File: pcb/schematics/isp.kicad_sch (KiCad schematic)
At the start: 23 parts, among them J3 Conn_02x07_Counter_Clockwise

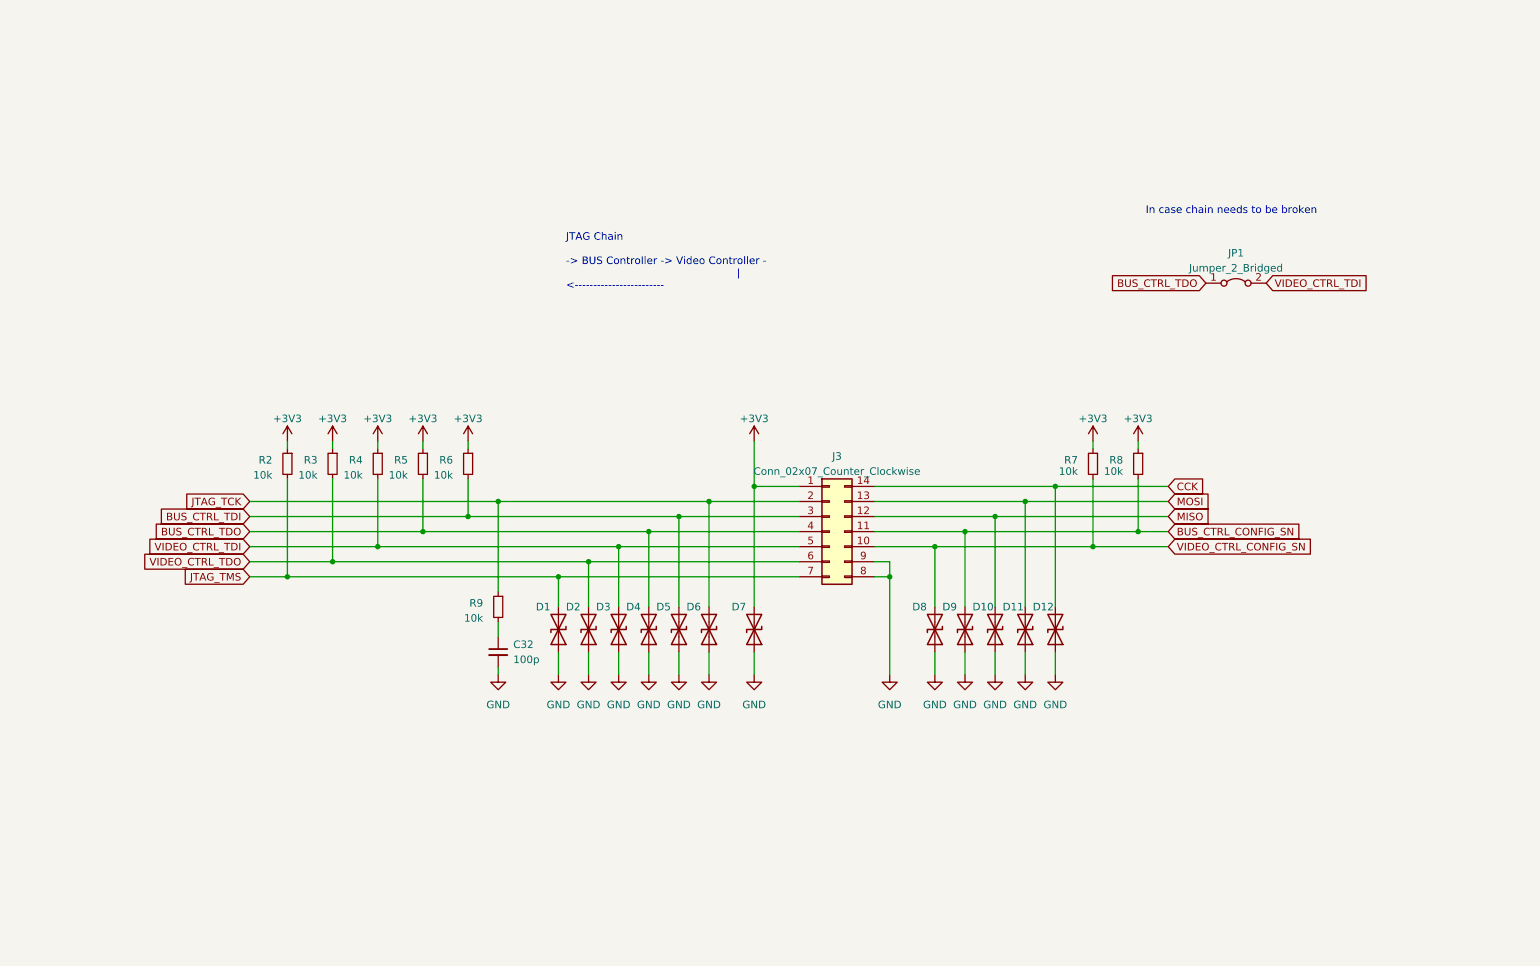
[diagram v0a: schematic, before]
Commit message: add the programming controller
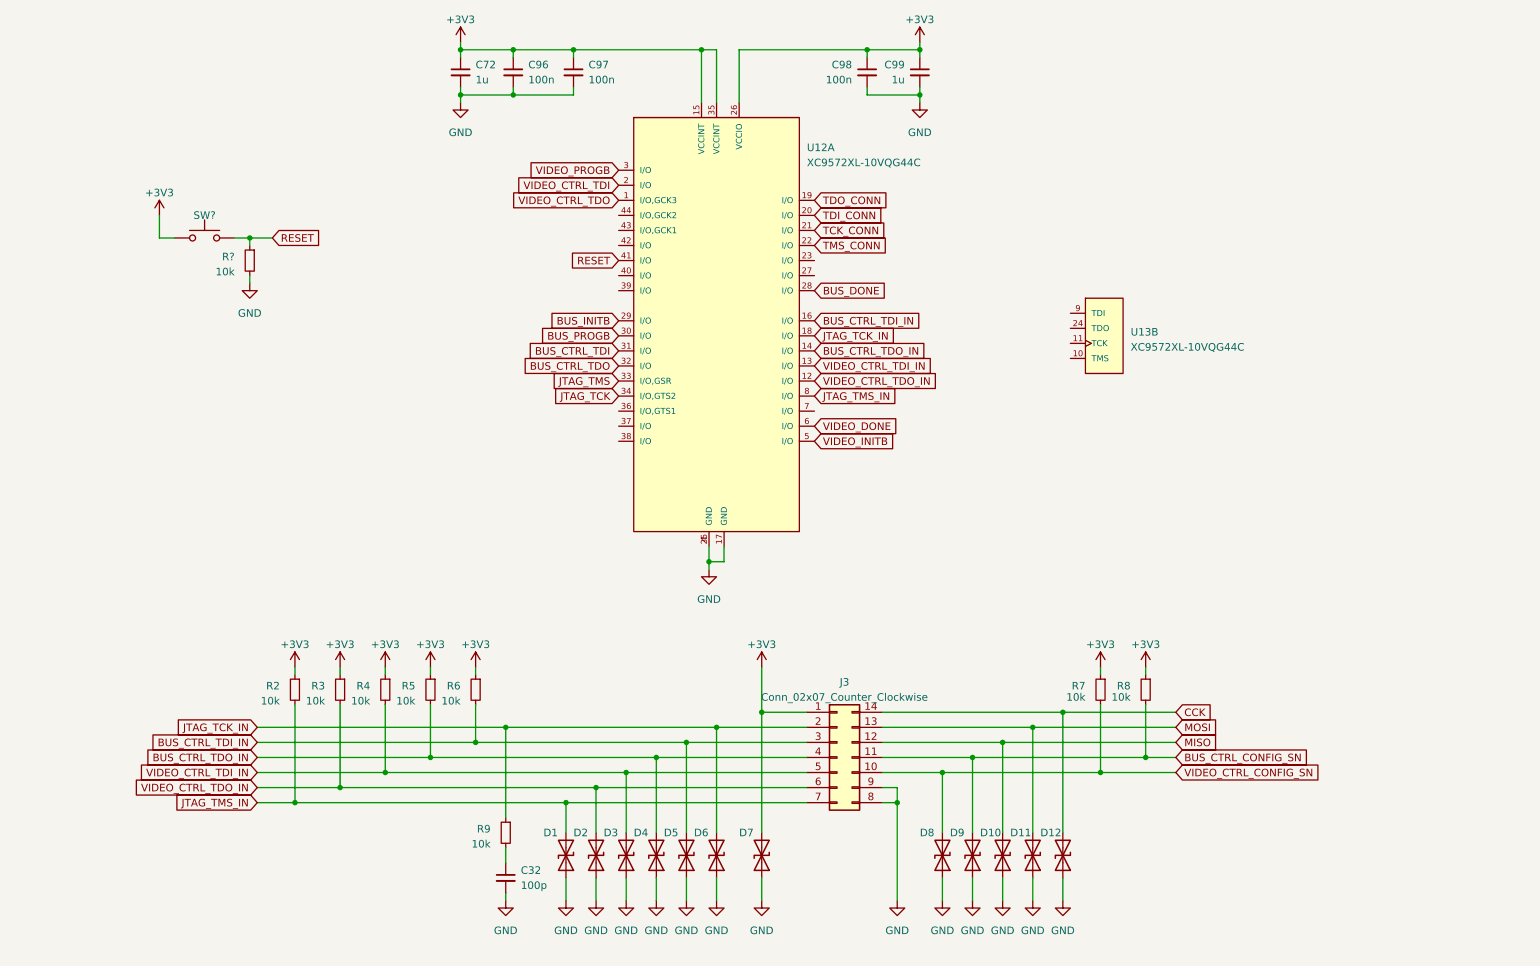
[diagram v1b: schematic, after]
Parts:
- removed JP1: Jumper_2_Bridged, Jumper:SolderJumper-2_P1.3mm_Bridged_RoundedPad1.0x1.5mm, symbol Jumper:Jumper_2_Bridged
- added C72, C99: 1u, Capacitor_SMD:C_0805_2012Metric, symbol Device:C_Small
- added C96, C97, C98: 100n, Capacitor_SMD:C_0603_1608Metric, symbol Device:C_Small
- added R?: 10k, Resistor_SMD:R_0603_1608Metric, symbol Device:R_Small
- added SW?: SW_Push, PTS636_SM43J_SMTR_LFS:SW_PTS636_SM43J_SMTR_LFS, symbol Switch:SW_Push
- added U12: XC9572XL-10VQG44C, XC9572XL-10VQG44C:Xilinx-XC9572XL-10VQG44C-Level_C, symbol XC9572XL-4VQG44C:XC9572XL-10VQG44C
- added U13: XC9572XL-10VQG44C, Xilinx-XC9572XL-10VQG44C-*, symbol XC9572XL-4VQG44C:XC9572XL-10VQG44C
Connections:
- net +3V3: now also C72.1, C96.1, C97.1, C98.1, C99.1, SW?.1, U12.15 (VCCINT), U12.26 (VCCIO), U12.35 (VCCINT)
- net BUS_CTRL_TDI: now also U12.31 (I/O); no longer D5.2 (A2), J3.3 (Pin_3), R6.2
- net BUS_CTRL_TDO: now also U12.32 (I/O); no longer D4.2 (A2), J3.4 (Pin_4), R5.2
- net GND: now also C72.2, C96.2, C97.2, C98.2, C99.2, R?.2, U12.17 (GND), U12.25 (GND), U12.4 (GND)
- net JTAG_TCK: now also U12.34 (I/O,GTS2); no longer D6.2 (A2), J3.2 (Pin_2), R9.1
- net JTAG_TMS: now also U12.33 (I/O,GSR); no longer D1.2 (A2), J3.7 (Pin_7), R2.2
- net VIDEO_CTRL_TDI: now also U12.2 (I/O); no longer D3.2 (A2), J3.5 (Pin_5), R4.2
- net VIDEO_CTRL_TDO: now also U12.1 (I/O,GCK3); no longer D2.2 (A2), J3.6 (Pin_6), R3.2
- new net BUS_CTRL_TDI_IN: D5.2 (A2), J3.3 (Pin_3), R6.2, U12.16 (I/O)
- new net BUS_CTRL_TDO_IN: D4.2 (A2), J3.4 (Pin_4), R5.2, U12.14 (I/O)
- new net BUS_DONE: U12.28 (I/O)
- new net BUS_INITB: U12.29 (I/O)
- new net BUS_PROGB: U12.30 (I/O)
- new net JTAG_TCK_IN: D6.2 (A2), J3.2 (Pin_2), R9.1, U12.18 (I/O)
- new net JTAG_TMS_IN: D1.2 (A2), J3.7 (Pin_7), R2.2, U12.8 (I/O)
- new net RESET: R?.1, SW?.2, U12.41 (I/O)
- new net TCK_CONN: U12.21 (I/O)
- new net TDI_CONN: U12.20 (I/O)
- new net TDO_CONN: U12.19 (I/O)
- new net TMS_CONN: U12.22 (I/O)
- new net VIDEO_CTRL_TDI_IN: D3.2 (A2), J3.5 (Pin_5), R4.2, U12.13 (I/O)
- new net VIDEO_CTRL_TDO_IN: D2.2 (A2), J3.6 (Pin_6), R3.2, U12.12 (I/O)
- new net VIDEO_DONE: U12.6 (I/O)
- new net VIDEO_INITB: U12.5 (I/O)
- new net VIDEO_PROGB: U12.3 (I/O)
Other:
- note removed: "In case chain needs to be broken"
- note removed: "JTAG Chain -> BUS Controller -> Video Controller - | <------------------------"
- moved on the sheet: C32, D1, D10, D11, D12, D2, D3, D4, D5, D6, D7, D8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

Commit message: add the programming controller's jtag to the connector
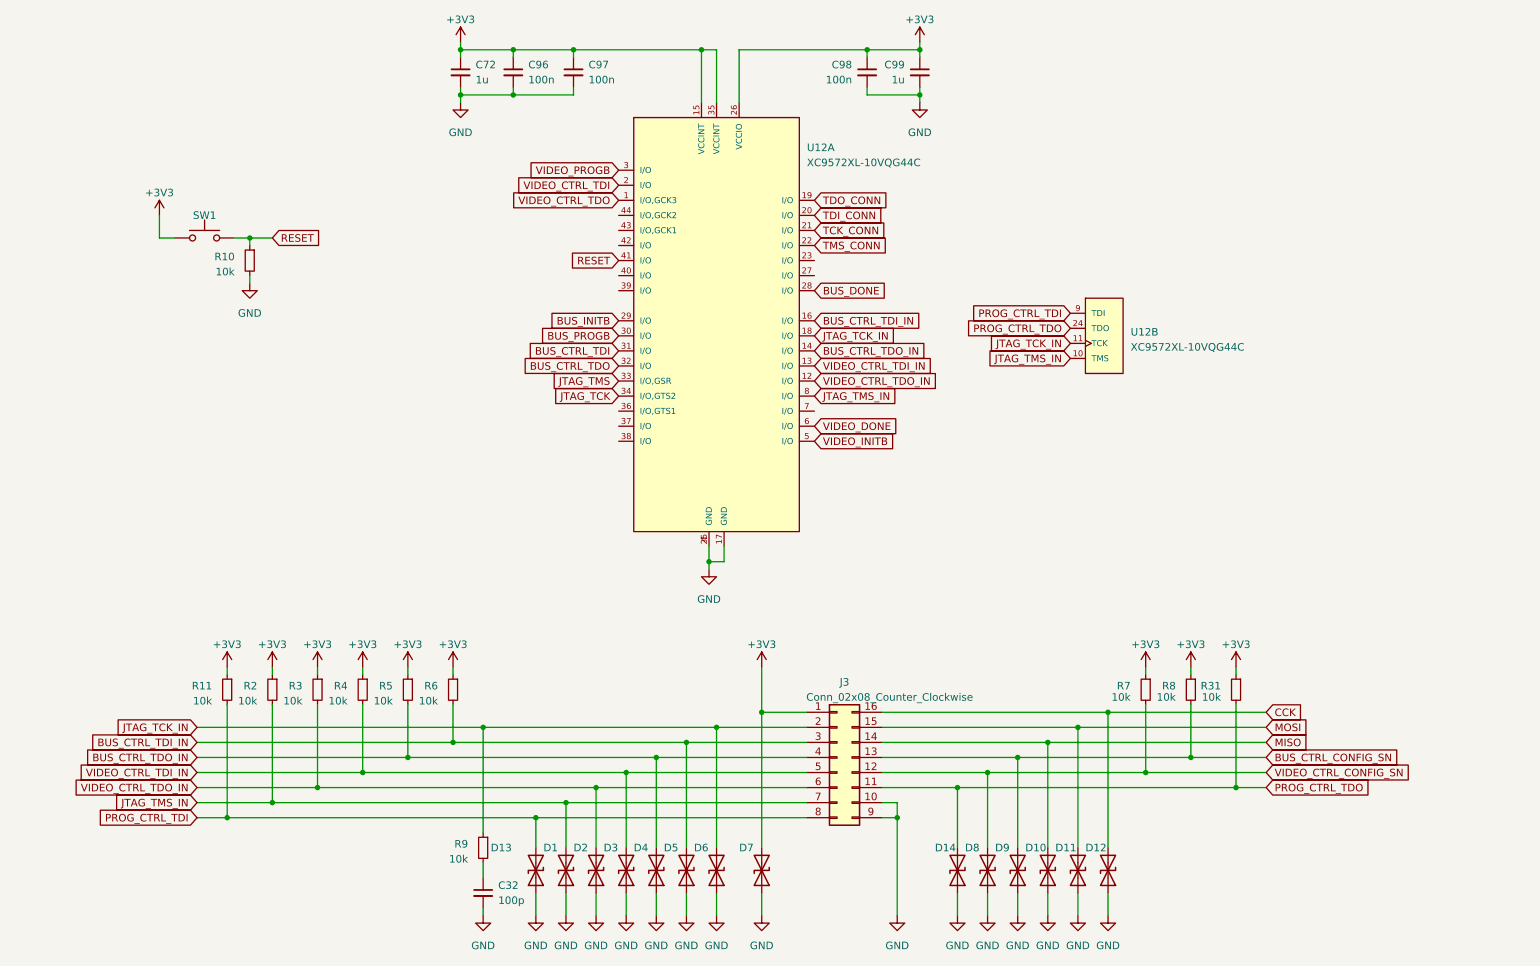
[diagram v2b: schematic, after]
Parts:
- removed J3: Conn_02x07_Counter_Clockwise, Connector_IDC:IDC-Header_2x07_P2.54mm_Vertical, symbol Connector_Generic:Conn_02x07_Counter_Clockwise
- added D13, D14: D_TVS, Diode_SMD:D_0603_1608Metric, symbol Device:D_TVS
- added J3: Conn_02x08_Counter_Clockwise, Connector_IDC:IDC-Header_2x08_P2.54mm_Vertical, symbol Connector_Generic:Conn_02x08_Counter_Clockwise
- added R11, R31: 10k, Resistor_SMD:R_0603_1608Metric, symbol Device:R_Small
- U12: renamed from U13; footprint Xilinx-XC9572XL-10VQG44C-* -> XC9572XL-10VQG44C:Xilinx-XC9572XL-10VQG44C-Level_C
- gave numbers to parts that had none: 2
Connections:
- net +3V3: now also J3.1 (Pin_1), R11.1, R31.1
- net BUS_CTRL_CONFIG_SN: now also J3.13 (Pin_13)
- net BUS_CTRL_TDI_IN: now also J3.3 (Pin_3)
- net BUS_CTRL_TDO_IN: now also J3.4 (Pin_4)
- net CCK: now also J3.16 (Pin_16)
- net GND: now also D13.1 (A1), D14.1 (A1), J3.10 (Pin_10), J3.9 (Pin_9)
- net JTAG_TCK_IN: now also U12.11 (TCK), J3.2 (Pin_2)
- net JTAG_TMS_IN: now also U12.10 (TMS), J3.7 (Pin_7)
- net MISO: now also J3.14 (Pin_14)
- net MOSI: now also J3.15 (Pin_15)
- net VIDEO_CTRL_CONFIG_SN: now also J3.12 (Pin_12)
- net VIDEO_CTRL_TDI_IN: now also J3.5 (Pin_5)
- net VIDEO_CTRL_TDO_IN: now also J3.6 (Pin_6)
- net PROG_CTRL_TDO: now reaches U12.24 (TDO)
- net PROG_CTRL_TDO: now also D14.2 (A2), J3.11 (Pin_11), R31.2
- net PROG_CTRL_TDI: now reaches U12.9 (TDI)
- net PROG_CTRL_TDI: now also D13.2 (A2), J3.8 (Pin_8), R11.2
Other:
- moved on the sheet: C32, D1, D10, D11, D12, D2, D3, D4, D5, D6, D7, D8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

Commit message: add shield
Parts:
- U: renamed from D9; value D_TVS -> (none); footprint Diode_SMD:D_0603_1608Metric -> (none)
- U: renamed from R8; value 10k -> (none); footprint Resistor_SMD:R_0603_1608Metric -> (none)
- U: renamed from R31; value 10k -> (none); footprint Resistor_SMD:R_0603_1608Metric -> (none)
- U: renamed from R9; value 10k -> (none); footprint Resistor_SMD:R_0603_1608Metric -> (none)
- U: renamed from D11; value D_TVS -> (none); footprint Diode_SMD:D_0603_1608Metric -> (none)
- U: renamed from R4; value 10k -> (none); footprint Resistor_SMD:R_0603_1608Metric -> (none)
- U: renamed from U12; value XC9572XL-10VQG44C -> (none); footprint XC9572XL-10VQG44C:Xilinx-XC9572XL-10VQG44C-Level_C -> (none)
- U: renamed from J3; value Conn_02x08_Counter_Clockwise -> (none); footprint Connector_IDC:IDC-Header_2x08_P2.54mm_Vertical -> (none)
- U: renamed from D10; value D_TVS -> (none); footprint Diode_SMD:D_0603_1608Metric -> (none)
- U: renamed from D4; value D_TVS -> (none); footprint Diode_SMD:D_0603_1608Metric -> (none)
- U: renamed from D8; value D_TVS -> (none); footprint Diode_SMD:D_0603_1608Metric -> (none)
- U: renamed from C96; value 100n -> (none); footprint Capacitor_SMD:C_0603_1608Metric -> (none)
- U: renamed from D7; value D_TVS -> (none); footprint Diode_SMD:D_0603_1608Metric -> (none)
- U: renamed from R2; value 10k -> (none); footprint Resistor_SMD:R_0603_1608Metric -> (none)
- U: renamed from R5; value 10k -> (none); footprint Resistor_SMD:R_0603_1608Metric -> (none)
- U: renamed from C72; value 1u -> (none); footprint Capacitor_SMD:C_0805_2012Metric -> (none)
- U: renamed from D5; value D_TVS -> (none); footprint Diode_SMD:D_0603_1608Metric -> (none)
- U: renamed from D2; value D_TVS -> (none); footprint Diode_SMD:D_0603_1608Metric -> (none)
- U: renamed from D3; value D_TVS -> (none); footprint Diode_SMD:D_0603_1608Metric -> (none)
- U: renamed from C99; value 1u -> (none); footprint Capacitor_SMD:C_0805_2012Metric -> (none)
- U: renamed from C32; value 100p -> (none); footprint Capacitor_SMD:C_0402_1005Metric -> (none)
- U: renamed from R10; value 10k -> (none); footprint Resistor_SMD:R_0603_1608Metric -> (none)
- U: renamed from D13; value D_TVS -> (none); footprint Diode_SMD:D_0603_1608Metric -> (none)
- U: renamed from R11; value 10k -> (none); footprint Resistor_SMD:R_0603_1608Metric -> (none)
- U: renamed from D1; value D_TVS -> (none); footprint Diode_SMD:D_0603_1608Metric -> (none)
- U: renamed from D6; value D_TVS -> (none); footprint Diode_SMD:D_0603_1608Metric -> (none)
- U: renamed from D14; value D_TVS -> (none); footprint Diode_SMD:D_0603_1608Metric -> (none)
- U: renamed from R6; value 10k -> (none); footprint Resistor_SMD:R_0603_1608Metric -> (none)
- U: renamed from C98; value 100n -> (none); footprint Capacitor_SMD:C_0603_1608Metric -> (none)
- U: renamed from C97; value 100n -> (none); footprint Capacitor_SMD:C_0603_1608Metric -> (none)
- U: renamed from SW1; value SW_Push -> (none); footprint PTS636_SM43J_SMTR_LFS:SW_PTS636_SM43J_SMTR_LFS -> (none)
- U: renamed from R3; value 10k -> (none); footprint Resistor_SMD:R_0603_1608Metric -> (none)
- U: renamed from R7; value 10k -> (none); footprint Resistor_SMD:R_0603_1608Metric -> (none)
- U: renamed from D12; value D_TVS -> (none); footprint Diode_SMD:D_0603_1608Metric -> (none)
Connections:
- net JTAG_TCK_IN: no longer U.11 (TCK)
- net JTAG_TMS_IN: no longer U.10 (TMS)
- net PROG_CTRL_TDI: no longer U.9 (TDI)
- net PROG_CTRL_TDO: no longer U.24 (TDO)
- new net: U.25 (GND), U.4 (GND)
